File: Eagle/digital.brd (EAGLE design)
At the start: 111.1 x 72.4 mm, 48 parts, among them J1 USB-B

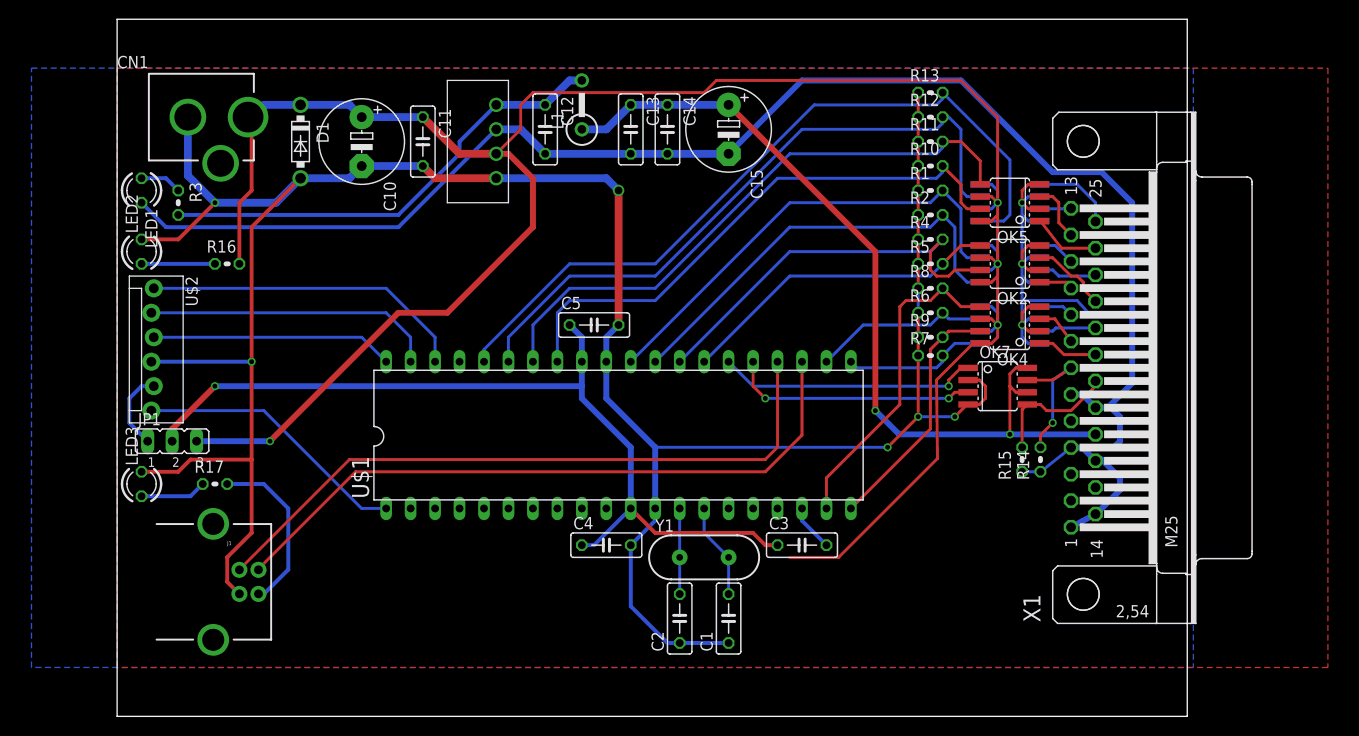
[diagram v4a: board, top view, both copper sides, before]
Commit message: Added 232 interface
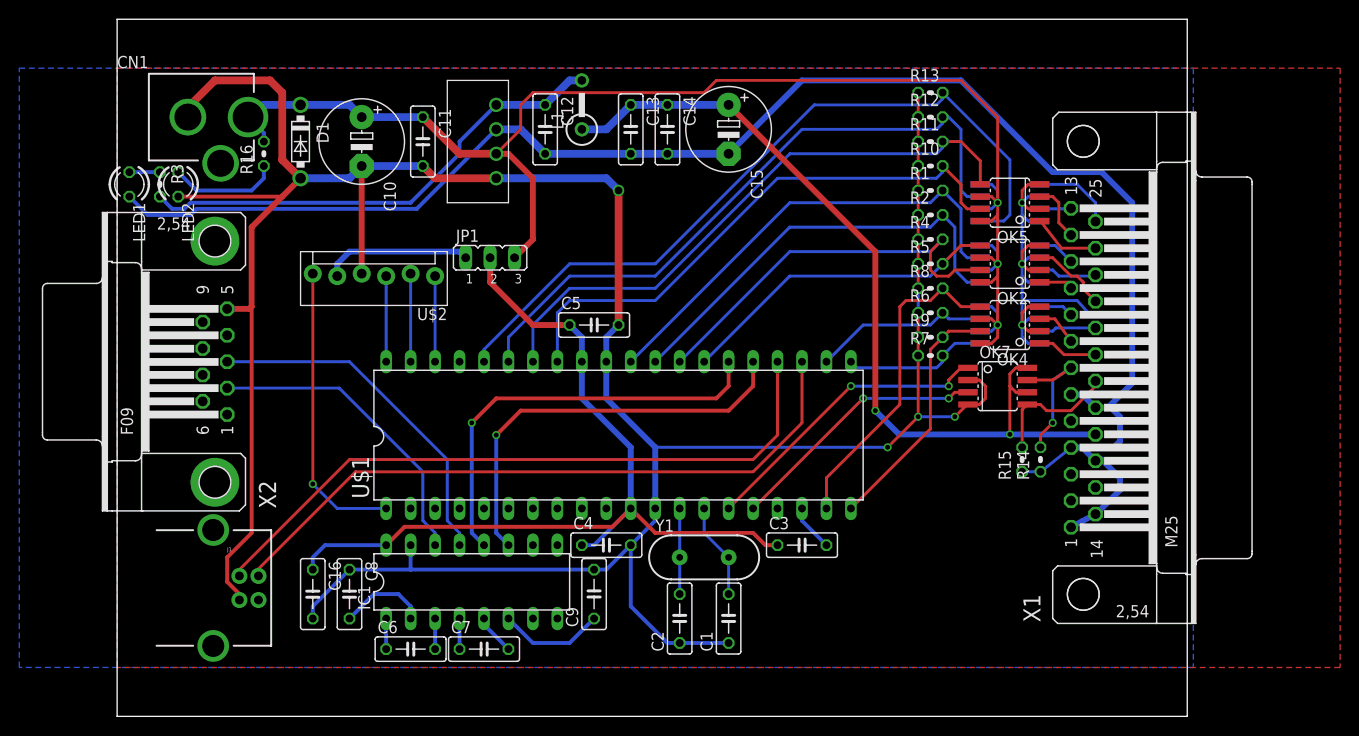
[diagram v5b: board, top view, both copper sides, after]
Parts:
- removed LED3: (no value), led:LED3MM
- removed R17: 1.65k, resistor:0204V
- added C16, C6, C7, C8, C9: 1uF, resistor:C050-025X075
- added IC1: MAX232, maxim:DIL16
- added X2: (no value), con-subd:F09HP
- C1, C2: value (none) -> 18pF
- J1: value USB-B -> USB+SHIELD
- moved JP1 38.1 mm to (38.7, 47.6)
- moved U$2 29.2 mm to (33.0, 45.7), turned to 180 degrees
- moved R16 12.0 mm to (15.2, 58.4), turned to 90 degrees
- moved LED2 7.96 mm to (6.35, 55.2), turned to 270 degrees
- moved R3 2.69 mm to (4.45, 55.2)
- moved LED1 1.42 mm to (1.27, 55.2)
- moved J1 0.63 mm to (12.7, 13.3)
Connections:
- removed net N$42: LED3.A, R17.1
- removed net N$43: J1.VBUS, R17.2
- new net N$44: IC1.11, U$1.25
- new net N$46: IC1.12, U$1.26
- new net N$47: C8.2, IC1.2
- new net N$48: C9.1, IC1.6
- new net N$49: C6.2, IC1.3
- new net N$50: C6.1, IC1.1
- new net N$51: C7.1, IC1.4
- new net N$52: C7.2, IC1.5
- new net N$53: IC1.13, X2.3
- new net N$54: IC1.14, X2.2
- net DGND: now also C16.2, C8.1, C9.2, IC1.15, J1.S1, J1.S2, X2.5; no longer LED3.K
- net N$39: now also U$1.15; no longer U$1.26
- net N$40: now also U$1.16; no longer U$1.25
- net N$45: now also C16.1, IC1.16
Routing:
- net +5V/2: track 242.0 -> 156.0 mm, vias 4 -> 3
- net N$46: track 0.00 -> 44.0 mm, vias 0 -> 1
- net N$44: track 0.00 -> 43.3 mm, vias 0 -> 1
- net N$53: track 0.00 -> 36.5 mm
- net DGND: track 265.0 -> 300.3 mm, vias 6 -> 4
- net N$54: track 0.00 -> 32.1 mm
- net N$6: track 33.9 -> 8.89 mm
- net N$7: track 30.5 -> 9.14 mm
- net N$43: track 17.9 -> 0.00 mm
- net N$8: track 25.2 -> 8.89 mm
- net N$48: track 0.00 -> 11.0 mm
- net N$47: track 0.00 -> 9.20 mm
- net N$10: track 8.30 -> 15.4 mm
- net N$42: track 6.88 -> 0.00 mm
- net N$52: track 0.00 -> 4.23 mm
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
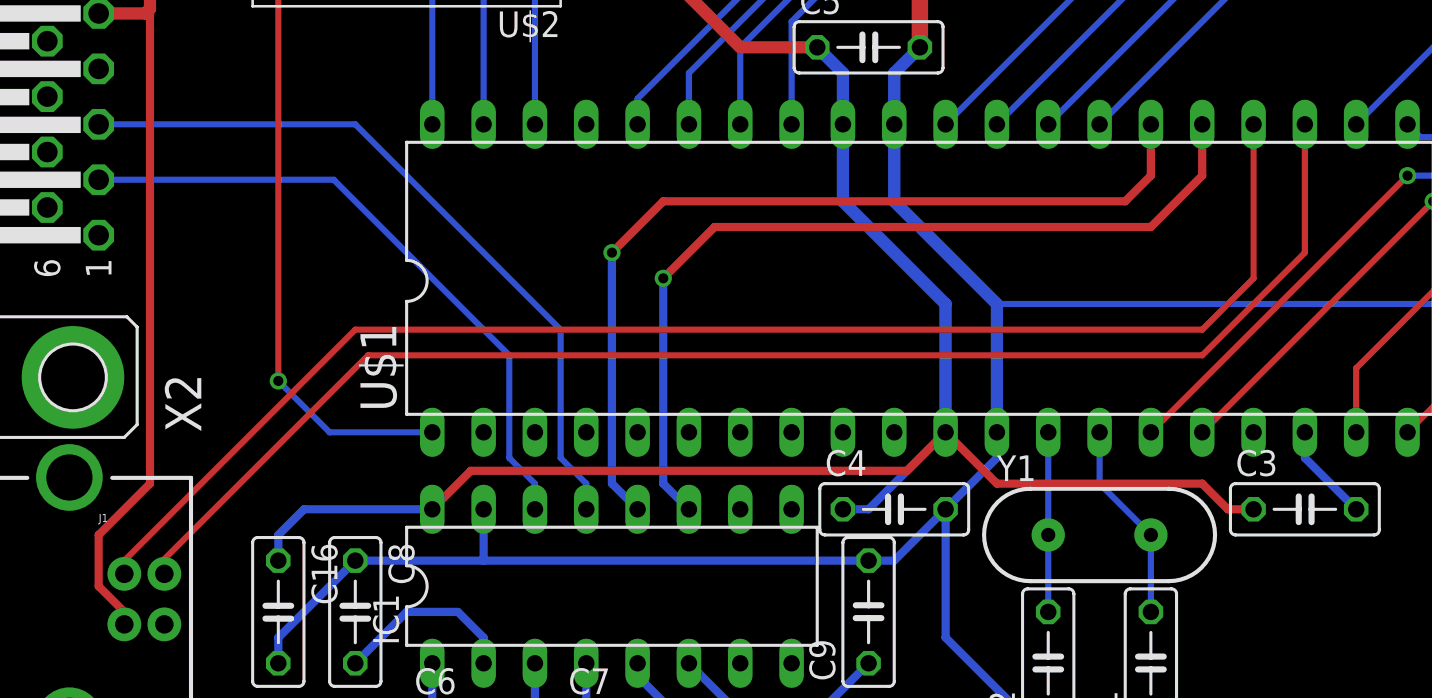
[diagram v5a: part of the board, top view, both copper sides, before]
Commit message: Changed USB to differential pair
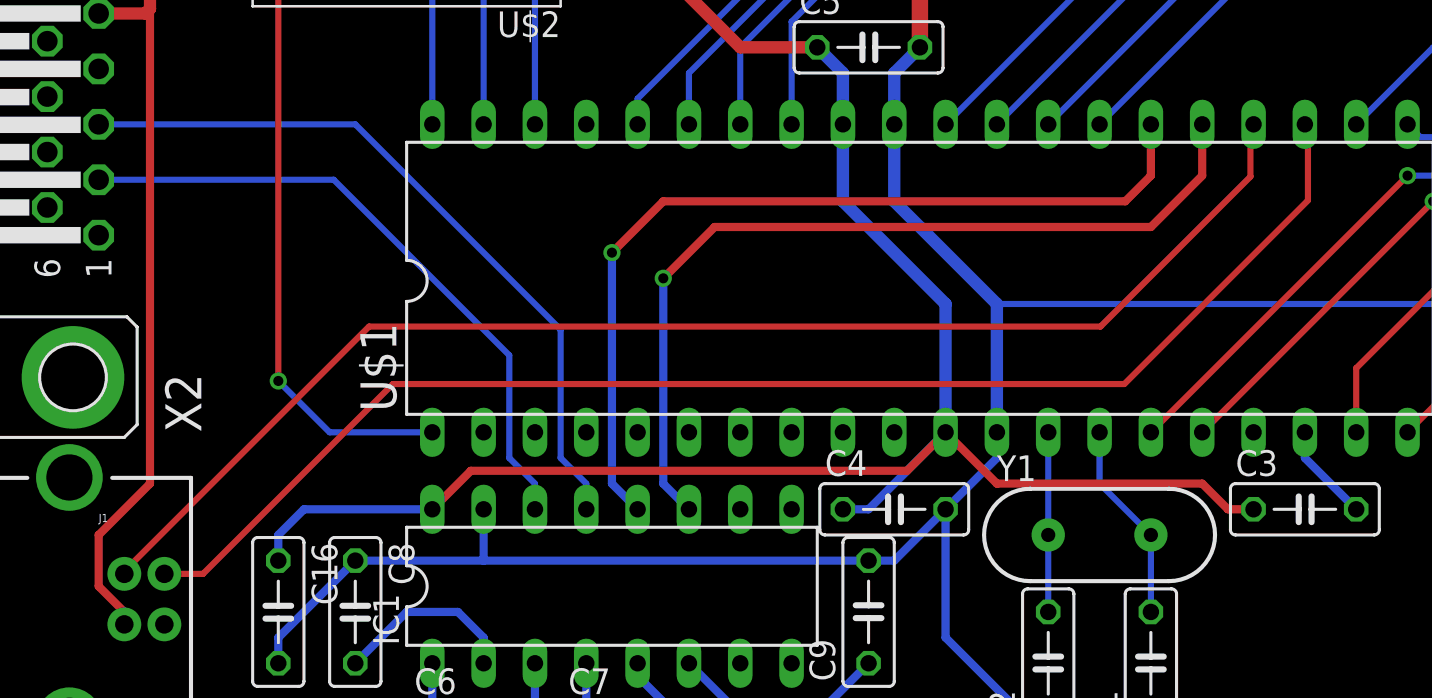
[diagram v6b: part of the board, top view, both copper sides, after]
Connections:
- net N$3 renamed USB_P
- net N$4 renamed USB_N
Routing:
- net USB_P: track 69.9 -> 66.7 mm
- net USB_N: track 69.9 -> 68.2 mm
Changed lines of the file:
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@@
 <class number="0" name="default" width="0" drill="0">
+</class>
+<class number="1" name="USB" width="0.3048" drill="0">
+<clearance class="1" value="2.54"/>
 </class>
 </classes>
@@
 <wire x1="27.94" y1="45.72" x2="27.94" y2="36.83" width="0.3048" layer="16"/>
 </signal>
-<signal name="N$3">
+<signal name="USB_P" class="1">
 <contactref element="J1" pad="D+"/>
 <contactref element="U$1" pad="24"/>
-<wire x1="68.58" y1="36.83" x2="68.58" y2="29.21" width="0.3048" layer="1"/>
-<wire x1="68.58" y1="29.21" x2="66.04" y2="26.67" width="0.3048" layer="1"/>
-<wire x1="24.13" y1="26.67" x2="66.04" y2="26.67" width="0.3048" layer="1"/>
-<wire x1="12.7" y1="15.24" x2="24.13" y2="26.67" width="0.3048" layer="1"/>
-<wire x1="12.7" y1="15.24" x2="12.7" y2="14.585" width="0.3048" layer="1"/>
-</signal>
-<signal name="N$4">
+<wire x1="12.7" y1="14.585" x2="12.7" y2="14.71158125" width="0.3048" layer="1"/>
+<wire x1="12.7" y1="14.71158125" x2="24.81081875" y2="26.8224" width="0.3048" layer="1"/>
+<wire x1="61.00581875" y1="26.8224" x2="24.81081875" y2="26.8224" width="0.3048" layer="1"/>
+<wire x1="61.00581875" y1="26.8224" x2="68.4276" y2="34.24418125" width="0.3048" layer="1"/>
+<wire x1="68.4276" y1="34.24418125" x2="68.4276" y2="36.83" width="0.3048" layer="1"/>
+<wire x1="68.4276" y1="36.83" x2="68.58" y2="36.83" width="0.3048" layer="1"/>
+</signal>
+<signal name="USB_N" class="1">
 <contactref element="U$1" pad="23"/>
 <contactref element="J1" pad="D-"/>
-<wire x1="71.12" y1="36.83" x2="71.12" y2="30.48" width="0.3048" layer="1"/>
-<wire x1="71.12" y1="30.48" x2="66.04" y2="25.4" width="0.3048" layer="1"/>
-<wire x1="24.765" y1="25.4" x2="66.04" y2="25.4" width="0.3048" layer="1"/>
-<wire x1="24.765" y1="25.4" x2="14.605" y2="15.24" width="0.3048" layer="1"/>
-<wire x1="14.605" y1="15.24" x2="14.7012" y2="15.24" width="0.3048" layer="1"/>
-<wire x1="14.7012" y1="15.24" x2="14.6812" y2="14.585" width="0.3048" layer="1"/>
+<wire x1="14.6812" y1="14.585" x2="16.59658125" y2="14.585" width="0.3048" layer="1"/>
+<wire x1="16.59658125" y1="14.585" x2="25.98918125" y2="23.9776" width="0.3048" layer="1"/>
+<wire x1="62.18418125" y1="23.9776" x2="25.98918125" y2="23.9776" width="0.3048" layer="1"/>
+<wire x1="62.18418125" y1="23.9776" x2="71.2724" y2="33.06581875" width="0.3048" layer="1"/>
+<wire x1="71.2724" y1="33.06581875" x2="71.2724" y2="36.83" width="0.3048" layer="1"/>
+<wire x1="71.2724" y1="36.83" x2="71.12" y2="36.83" width="0.3048" layer="1"/>
 </signal>
 <signal name="N$9">

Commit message: Added RTS
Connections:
- new net N$3: IC1.8, X2.7
- new net N$4: IC1.9, U$1.17
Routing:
- net N$3: track 0.00 -> 50.2 mm, vias 0 -> 1
- net N$4: track 0.00 -> 30.6 mm, vias 0 -> 2
- net DGND: track 300.3 -> 300.8 mm
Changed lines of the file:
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@@
 </class>
 <class number="1" name="USB" width="0.3048" drill="0">
-<clearance class="1" value="2.54"/>
+<clearance class="1" value="0.254"/>
 </class>
 </classes>
@@
 <wire x1="57.15" y1="7.62" x2="53.34" y2="11.43" width="0.4064" layer="16"/>
 <wire x1="53.34" y1="11.43" x2="53.34" y2="17.78" width="0.4064" layer="16"/>
-<wire x1="12.7" y1="12.085" x2="12.68" y2="12.72" width="0.4064" layer="1"/>
-<wire x1="12.68" y1="12.72" x2="11.43" y2="13.97" width="0.4064" layer="1"/>
-<wire x1="11.43" y1="13.97" x2="11.43" y2="16.51" width="0.4064" layer="1"/>
-<wire x1="11.43" y1="16.51" x2="13.97" y2="19.05" width="0.4064" layer="1"/>
+<wire x1="12.7" y1="12.085" x2="12.68" y2="12.085" width="0.4064" layer="1"/>
+<wire x1="12.68" y1="12.085" x2="10.795" y2="13.97" width="0.4064" layer="1"/>
+<wire x1="10.795" y1="13.97" x2="10.795" y2="15.875" width="0.4064" layer="1"/>
+<wire x1="10.795" y1="15.875" x2="13.97" y2="19.05" width="0.4064" layer="1"/>
 <wire x1="13.97" y1="19.05" x2="13.97" y2="42.545" width="0.4064" layer="1"/>
 <wire x1="13.97" y1="42.545" x2="13.97" y2="50.8" width="0.6096" layer="1"/>
@@
 <wire x1="24.13" y1="36.83" x2="11.43" y2="36.83" width="0.3048" layer="16"/>
 </signal>
+<signal name="N$3">
+<contactref element="X2" pad="7"/>
+<contactref element="IC1" pad="8"/>
+<wire x1="8.89" y1="35.4584" x2="8.89" y2="34.925" width="0.3048" layer="16"/>
+<wire x1="8.89" y1="34.925" x2="10.795" y2="33.02" width="0.3048" layer="16"/>
+<wire x1="10.795" y1="33.02" x2="13.335" y2="33.02" width="0.3048" layer="16"/>
+<wire x1="13.335" y1="33.02" x2="17.145" y2="29.21" width="0.3048" layer="16"/>
+<wire x1="17.145" y1="29.21" x2="17.145" y2="24.765" width="0.3048" layer="16"/>
+<wire x1="17.145" y1="24.765" x2="22.86" y2="19.05" width="0.3048" layer="16"/>
+<via x="22.86" y="19.05" extent="1-16" drill="0.5"/>
+<wire x1="22.86" y1="19.05" x2="28.575" y2="13.335" width="0.3048" layer="1"/>
+<wire x1="28.575" y1="13.335" x2="42.545" y2="13.335" width="0.3048" layer="1"/>
+<wire x1="42.545" y1="13.335" x2="45.72" y2="10.16" width="0.3048" layer="1"/>
+</signal>
+<signal name="N$4">
+<contactref element="IC1" pad="9"/>
+<contactref element="U$1" pad="17"/>
+<wire x1="68.58" y1="21.59" x2="64.77" y2="25.4" width="0.3048" layer="16"/>
+<wire x1="64.77" y1="25.4" x2="59.69" y2="25.4" width="0.3048" layer="16"/>
+<via x="59.69" y="25.4" extent="1-16" drill="0.5"/>
+<wire x1="59.69" y1="25.4" x2="50.8" y2="25.4" width="0.3048" layer="1"/>
+<via x="50.8" y="25.4" extent="1-16" drill="0.5"/>
+<wire x1="50.8" y1="25.4" x2="48.26" y2="25.4" width="0.3048" layer="16"/>
+<wire x1="48.26" y1="25.4" x2="46.99" y2="24.13" width="0.3048" layer="16"/>
+<wire x1="46.99" y1="24.13" x2="46.99" y2="19.05" width="0.3048" layer="16"/>
+<wire x1="46.99" y1="19.05" x2="45.72" y2="17.78" width="0.3048" layer="16"/>
+</signal>
 </signals>

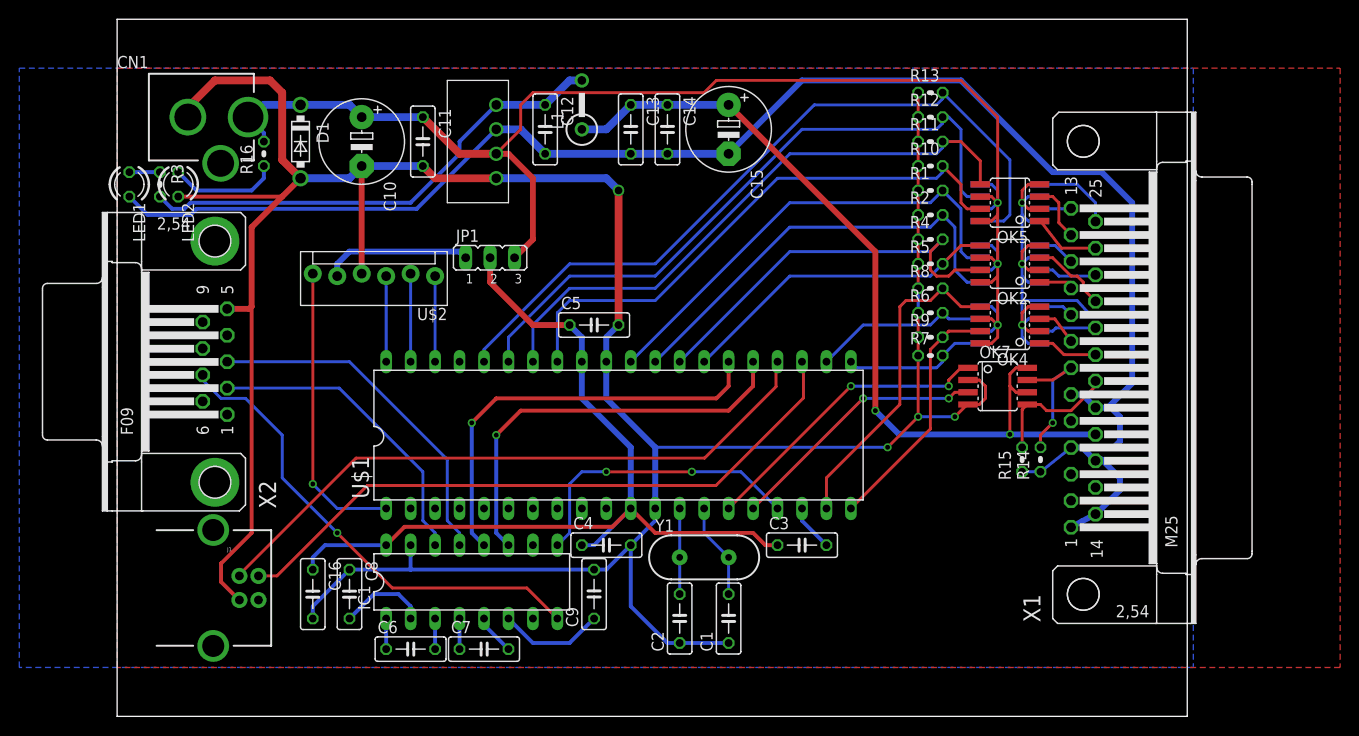
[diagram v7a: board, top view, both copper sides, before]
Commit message: Shrunk boards
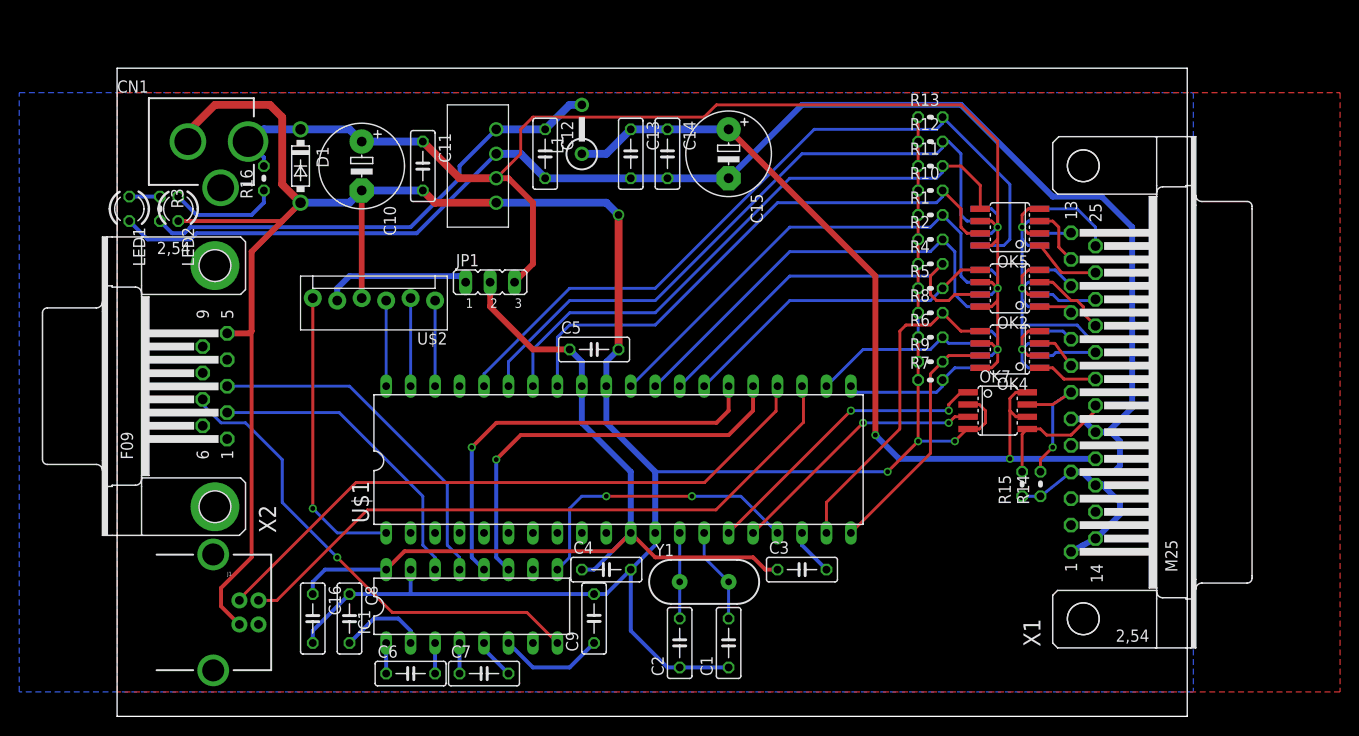
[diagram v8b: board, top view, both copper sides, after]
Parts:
- moved OK5 2.54 mm to (92.7, 50.8)
- moved OK6 2.54 mm to (92.7, 50.8)
- moved R7 2.54 mm to (84.5, 34.9)
- moved R8 2.54 mm to (84.5, 41.9)
- moved R14 2.54 mm to (95.9, 24.1)
- moved R15 2.54 mm to (94.0, 24.1)
- moved C3 2.54 mm to (71.1, 15.2)
- moved C4 2.54 mm to (50.8, 15.2)
- moved IC1 2.54 mm to (36.8, 11.4)
- moved J1 2.54 mm to (12.7, 10.8)
- moved Y1 2.54 mm to (61.0, 14.0)
- moved C1 2.54 mm to (63.5, 7.62)
- moved C2 2.54 mm to (58.4, 7.62)
- moved C6 2.54 mm to (30.5, 4.45)
- moved C7 2.54 mm to (38.1, 4.45)
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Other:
- board size 111.1 x 72.4 mm -> 111.1 x 67.3 mm
